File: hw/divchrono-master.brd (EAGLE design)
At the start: 100 x 80 mm, 47 parts, among them U1 TPS562200DDCR, U2 1364, U3 74HC595D

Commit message: Finished display interface and started master board schematic finalization.
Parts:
- added Q1, Q2, Q3, Q4: BSS138, SparkFun-DiscreteSemi:SOT23-3
- added R18, R19, R20, R21, R22, R23, R24, R25: 10k, rcl:R1206
- moved J1 6.35 mm to (5.08, 11.4)
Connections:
- removed net DISPLAY_BLANK: J2.12
- removed net DISPLAY_CLK: J2.18
- removed net DISPLAY_DAT: J2.16
- removed net DISPLAY_LAT: J2.10
- removed net N$10: J3.3
- removed net N$11: J3.5
- removed net N$12: J3.7
- removed net N$13: J3.9
- new net DISPLAY_BLANK_12V: J3.3, Q3.3, R23.1
- new net DISPLAY_BLANK_3V3: J2.12, Q3.2, R22.1
- new net DISPLAY_CLK_12V: J3.9, Q4.3, R25.1
- new net DISPLAY_CLK_3V3: J2.18, Q4.2, R24.1
- new net DISPLAY_DAT_12V: J3.7, Q2.3, R21.1
- new net DISPLAY_DAT_3V3: J2.16, Q2.2, R20.1
- new net DISPLAY_LAT_12V: J3.5, Q1.3, R19.1
- new net DISPLAY_LAT_3V3: J2.10, Q1.2, R18.1
- net +12V: now also R19.2, R21.2, R23.2, R25.2
- net +3V3: now also Q1.1, Q2.1, Q3.1, Q4.1, R18.2, R20.2, R22.2, R24.2

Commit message: Final modifications before master board layout. Changed status LED hookup to allow more streamlined part positioning.
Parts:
- moved Q4 347.2 mm to (52.1, 54.6)
- moved R25 345.0 mm to (52.1, 59.7), turned to 180 degrees
- moved Q3 331.3 mm to (40.6, 40.6)
- moved R21 330.8 mm to (40.6, 59.7)
- moved R23 320.6 mm to (40.6, 44.5)
- moved R24 319.3 mm to (10.2, 47.0), turned to 180 degrees
- moved R19 312.0 mm to (52.1, 45.7)
- moved Q2 305.0 mm to (40.6, 54.6)
- moved R22 303.8 mm to (10.2, 36.8), turned to 180 degrees
- moved R20 296.7 mm to (10.2, 41.9), turned to 180 degrees
- moved Q1 296.3 mm to (52.1, 40.6)
- moved R18 274.3 mm to (10.2, 30.5)
- moved R17 264.4 mm to (48.3, 10.2), turned to 270 degrees
- moved R16 258.1 mm to (44.5, 10.2), turned to 270 degrees
- moved R15 251.8 mm to (40.6, 10.2), turned to 270 degrees
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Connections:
- removed net N$23: D5.C, R14.1
- removed net N$24: D6.C, R15.1
- removed net N$25: D7.C, R16.1
- removed net N$26: D8.C, R17.1
- new net N$10: D8.A, R17.2
- new net N$11: D7.A, R16.2
- new net N$12: D6.A, R15.2
- new net N$13: D5.A, R14.2
- net GND: now also D1.C, D2.C, D3.C, D4.C, D5.C, D6.C, D7.C, D8.C; no longer R10.2, R11.2, R12.2, R13.2, R14.2, R15.2, R16.2, R17.2
- net N$14: now also R11.1; no longer D2.A
- net N$15: now also R10.1; no longer D1.A
- net N$16: now also R15.1; no longer D6.A
- net N$17: now also R16.1; no longer D7.A
- net N$18: now also R17.1; no longer D8.A
- net N$19: now also D4.A, R13.2; no longer D1.C, R10.1
- net N$20: now also D3.A, R12.2; no longer D2.C, R11.1
- net N$21: now also D2.A, R11.2; no longer D3.C, R12.1
- net N$22: now also D1.A, R10.2; no longer D4.C, R13.1
- net N$7: now also R14.1; no longer D5.A
- net N$8: now also R13.1; no longer D4.A
- net N$9: now also R12.1; no longer D3.A
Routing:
- added copper zone on layer 16, net +12V
- added copper zone on layer 16, net +3V3
- added copper zone on layer 1, net GND
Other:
- board size 100 x 80 mm -> 95.2 x 76.2 mm

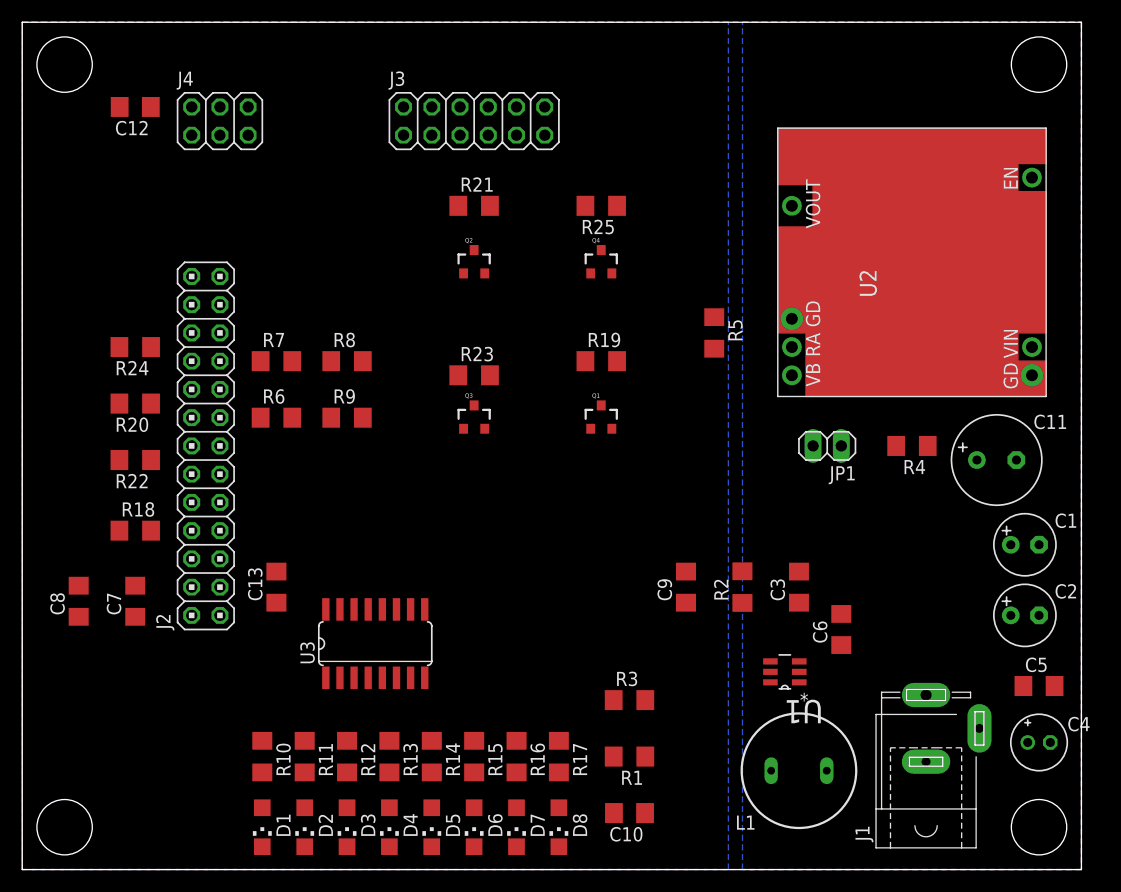
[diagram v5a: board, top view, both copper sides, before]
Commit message: Finished initial layout for master board, minor schematic and BOM changes.
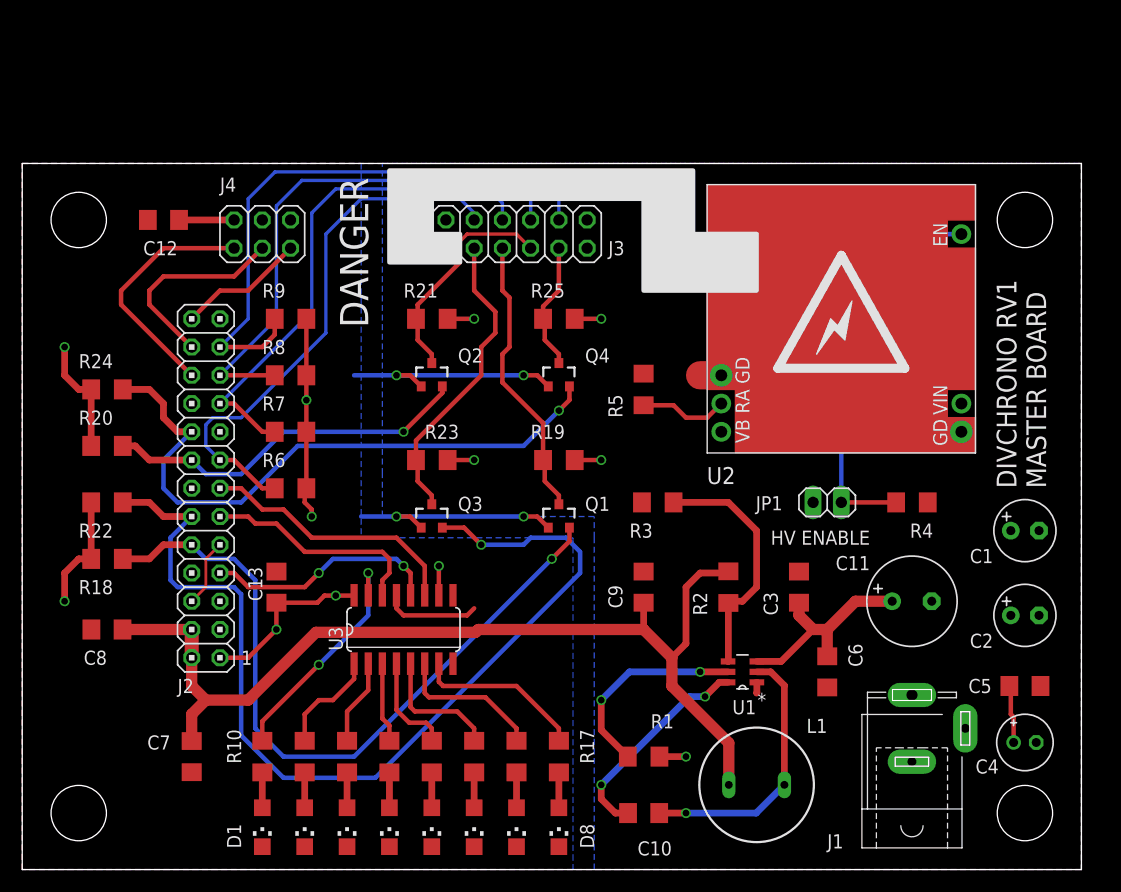
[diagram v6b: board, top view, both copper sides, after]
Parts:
- added U$1: (no value), dicons:ICON_DANGER
- added U$2: (no value), dicons:ICON_BOLT-L
- moved R3 18.0 mm to (57.1, 33.0)
- moved C7 14.9 mm to (15.2, 10.2), turned to 270 degrees
- moved C11 14.8 mm to (80.0, 24.1)
- moved J3 10.9 mm to (44.5, 57.1)
- moved J4 10.9 mm to (21.6, 57.1)
- moved Q2 10.9 mm to (36.8, 44.5)
- moved Q4 10.9 mm to (48.3, 44.5)
- moved R21 10.9 mm to (36.8, 49.5)
- moved R25 10.9 mm to (48.3, 49.5), turned to 0 degrees
- moved C12 10.5 mm to (12.7, 58.4)
- moved R9 10.2 mm to (24.1, 49.5)
- moved Q1 9.67 mm to (48.3, 31.8)
- moved Q3 9.67 mm to (36.8, 31.8)
- moved R19 9.67 mm to (48.3, 36.8)
- moved R23 8.52 mm to (36.8, 36.8)
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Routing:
- net +3V3: track 0.00 -> 103.0 mm, vias 0 -> 11
- net +5V: track 0.00 -> 90.1 mm
- net DISPLAY_BLANK_3V3: track 0.00 -> 88.2 mm, vias 0 -> 1
- net DISPLAY_LAT_3V3: track 0.00 -> 65.6 mm, vias 0 -> 1
- net DISPLAY_CLK_3V3: track 0.00 -> 56.7 mm, vias 0 -> 1
- net BUTTON_DOWN: track 0.00 -> 53.9 mm
- net BUTTON_UP: track 0.00 -> 48.7 mm
- net BUTTON_LEFT: track 0.00 -> 48.6 mm
- net BUTTON_RIGHT: track 0.00 -> 46.6 mm
- net HV: track 0.00 -> 41.4 mm
- net +12V: track 0.00 -> 37.1 mm, vias 0 -> 5
- net N$3: track 0.00 -> 35.4 mm
- net DISPLAY_DAT_3V3: track 0.00 -> 33.4 mm, vias 0 -> 1
- net DISPLAY_BLANK_12V: track 0.00 -> 27.4 mm
- net DISPLAY_LAT_12V: track 0.00 -> 25.7 mm
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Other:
- board size 95.2 x 76.2 mm -> 95.2 x 63.5 mm
- board text added: "1"
- board text added: "DANGER"
- board text added: "DIVCHRONO RV1 MASTER BOARD"
- board text added: "HV ENABLE"
